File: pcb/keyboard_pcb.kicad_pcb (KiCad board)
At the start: 2 copper layers, 142.9 x 98.6 mm, 25 parts, among them J1 TRRS, K00 KEYSW, K01 KEYSW, K02 KEYSW, K03 KEYSW, K04 KEYSW, K05 KEYSW, K10 KEYSW, K11 KEYSW, K12 KEYSW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

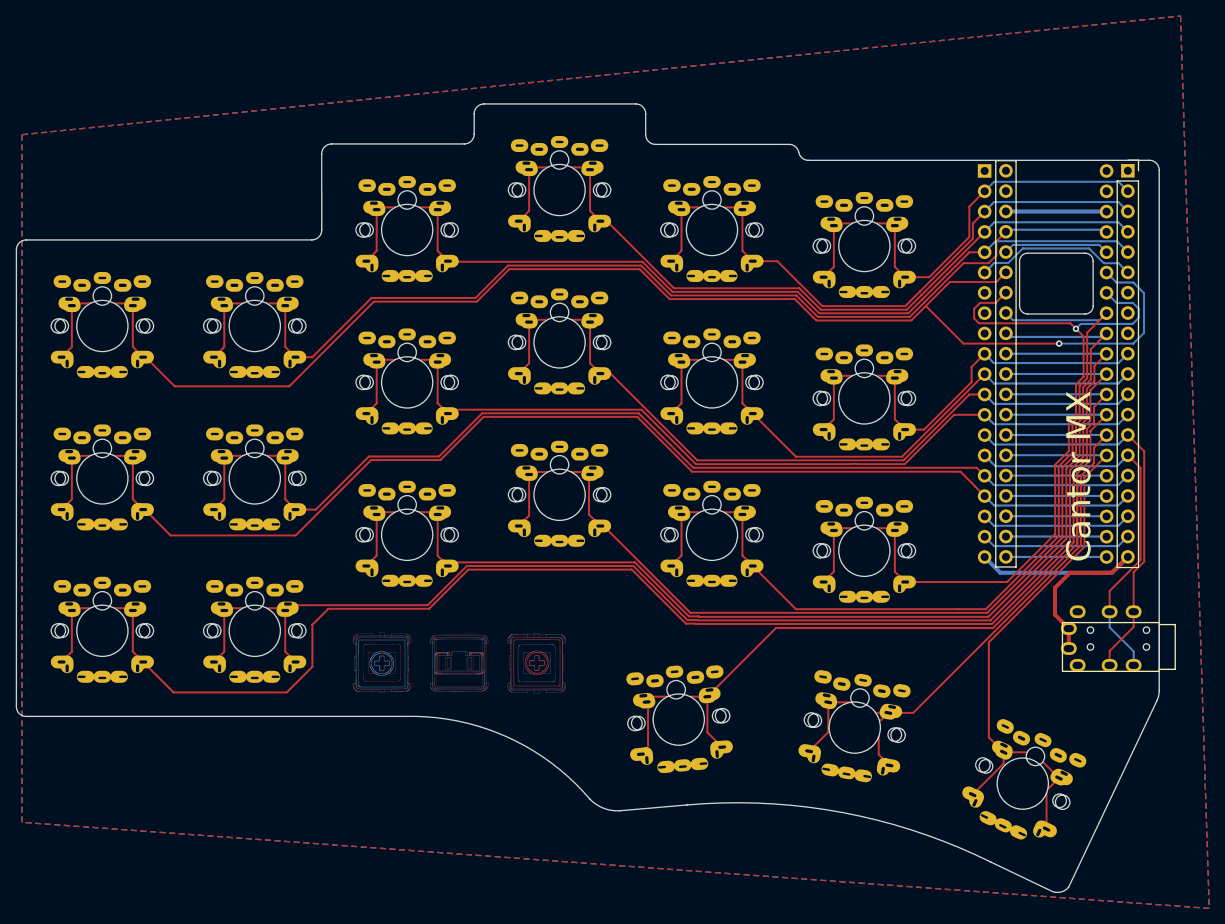
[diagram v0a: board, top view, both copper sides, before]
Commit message: Fixed LH traces after footprint rework
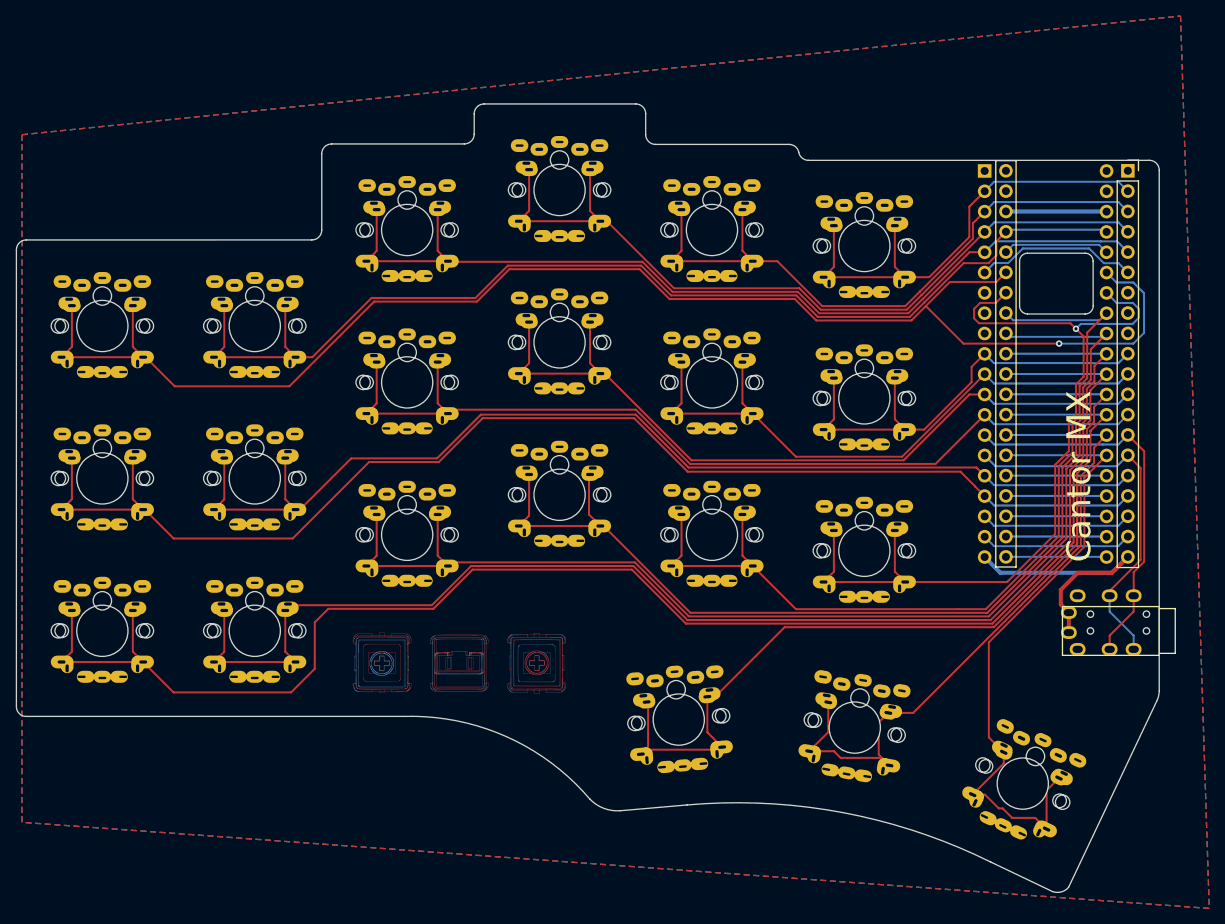
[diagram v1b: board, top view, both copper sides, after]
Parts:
- moved J1 2.00 mm to (200.9, 108.1)
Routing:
- net /k30: track 113.7 -> 117.3 mm
- net /k20: track 188.1 -> 191.5 mm
- net /k10: track 156.5 -> 159.9 mm
- net +3V3: track 51.1 -> 48.0 mm
- net /k24: track 108.9 -> 112.1 mm
- net /k05: track 56.5 -> 59.6 mm
- net /k25: track 103.4 -> 106.6 mm
- net /k15: track 54.9 -> 58.0 mm
- net /k14: track 75.4 -> 78.5 mm
- net /k13: track 95.8 -> 99.0 mm
- net /k04: track 77.2 -> 80.3 mm
- net /k03: track 96.5 -> 99.7 mm
- net /k02: track 113.0 -> 116.1 mm
- net /k01: track 134.7 -> 137.8 mm
- net /k00: track 182.0 -> 185.2 mm
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
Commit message: Updated readme
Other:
- board text added: "Cantor MX rev1.2 by JellyTitan"
- board text removed: "Cantor MX rev1.1 by JellyTitan"

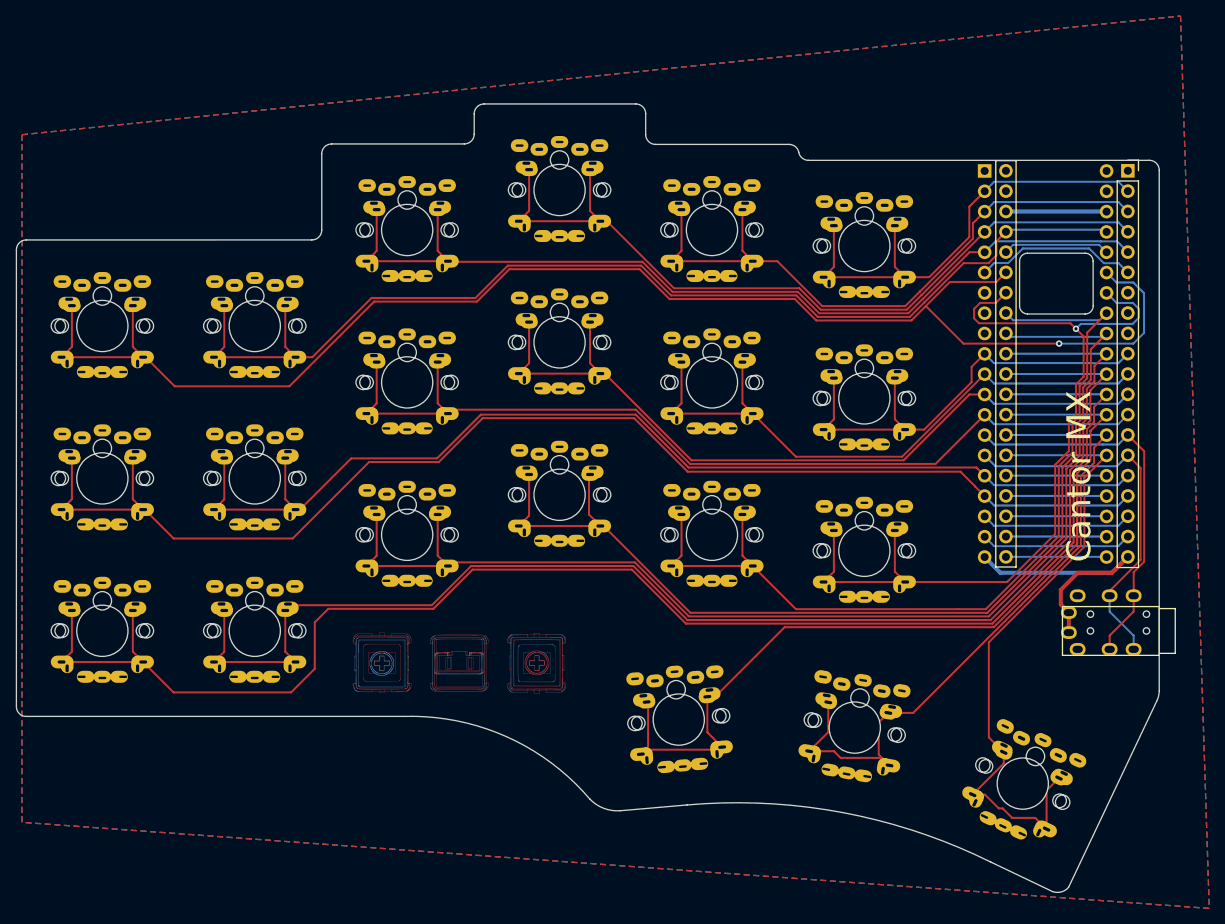
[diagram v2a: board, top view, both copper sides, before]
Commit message: Swapped in 'kitckitchen sink' switch footprints Updated trrs jack poke-yoke Blackpill masking
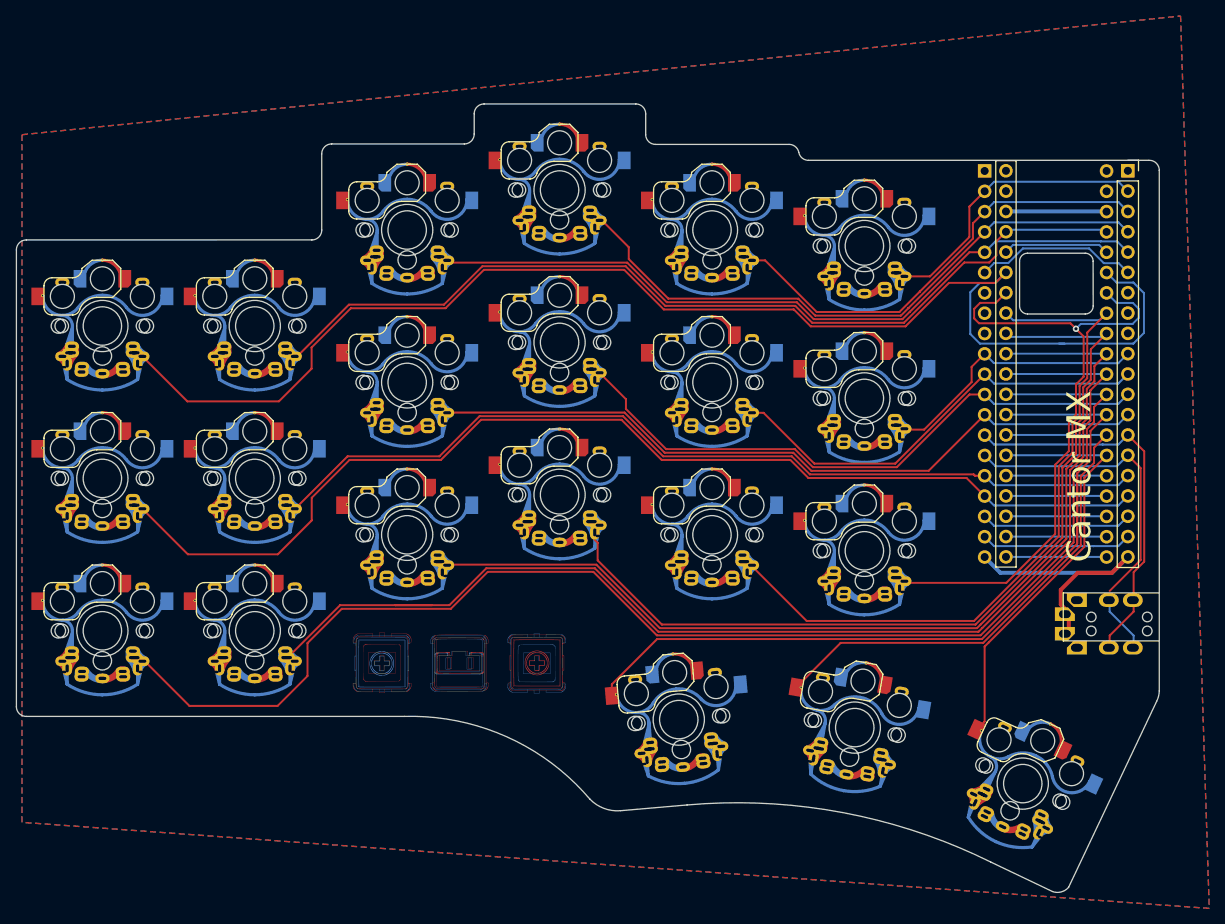
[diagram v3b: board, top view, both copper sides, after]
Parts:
- J1: footprint ergodonk_kicad_library:Cantor_DS_TRRS-PJ-320A -> ergodonk_kicad_library:MJ-4PP-9_CANTOR_KITCHEN_SINK
- K00, K01, K02, K03, K04, K05, K10, K11, K12, K13, K14, K15, K20, K21, K22, K23, K24, K25, K30, K31, K32: footprint ergodonk_kicad_library:CherryMX_ChocV2_1u -> ergodonk_kicad_library:ALL LOWs CANTOR
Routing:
- net /k32: track 81.5 -> 54.1 mm
- net /k15: track 58.0 -> 33.9 mm
- net /k05: track 59.6 -> 35.6 mm
- net /k11: track 137.2 -> 113.2 mm
- net /k25: track 106.6 -> 82.7 mm
- net /k01: track 137.8 -> 114.3 mm
- net /k04: track 80.3 -> 57.0 mm
- net /k14: track 78.5 -> 55.2 mm
- net /k12: track 115.0 -> 92.0 mm
- net /k24: track 112.1 -> 89.4 mm
- net /k20: track 191.5 -> 168.9 mm
- net /k03: track 99.7 -> 77.2 mm
- net /k22: track 146.2 -> 123.7 mm
- net /k13: track 99.0 -> 77.2 mm
- net /k02: track 116.1 -> 94.9 mm
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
